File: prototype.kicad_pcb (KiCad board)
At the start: 2 copper layers, 101.5 x 83 mm, 20 parts, among them CON1 SNES-CONN, IC1 SN74LVC4245A, IC2 SN74LVC4245A, IC3 SN74LVC4245A, IC4 SN74LVC4245A, IC5 SN74LVC4245A, IC6 SN74LVC4245A, IC7 SN74LVC4245A, U1 AMS1117-3.3

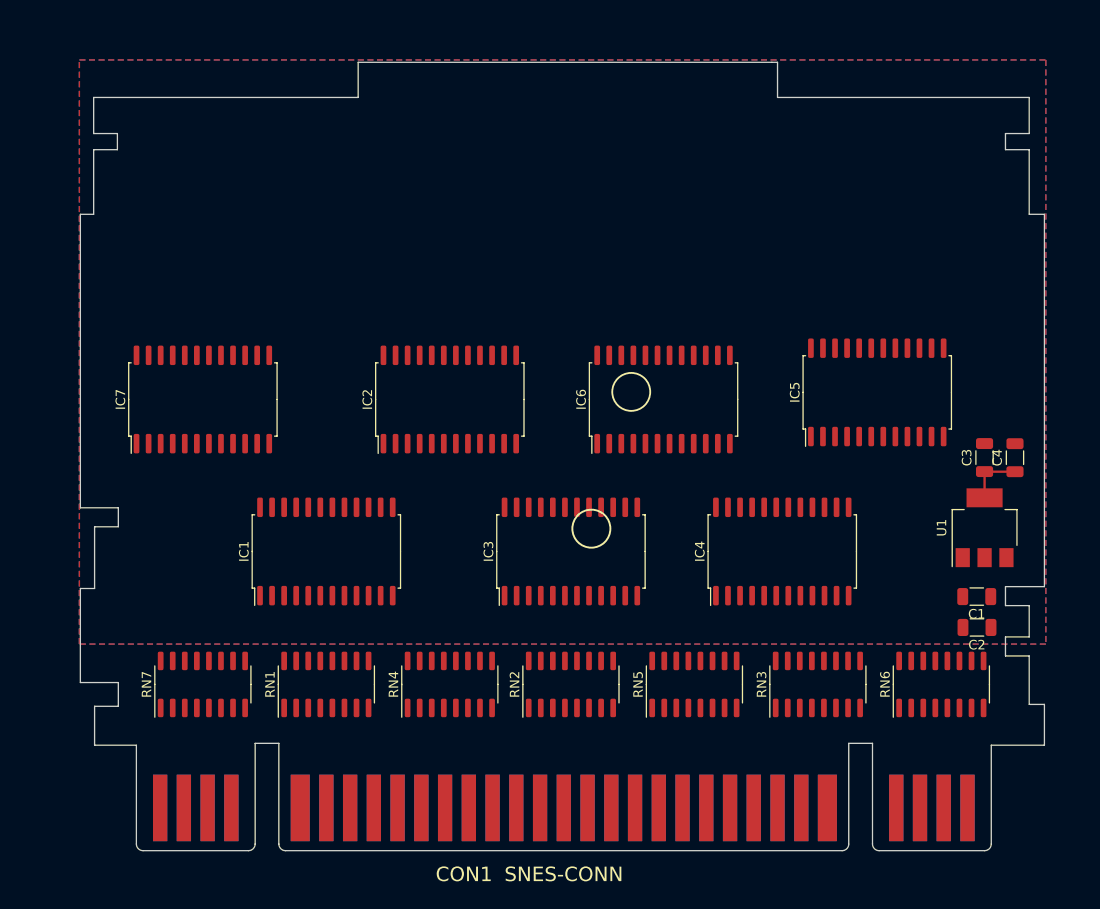
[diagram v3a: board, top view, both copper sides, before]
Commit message: Redesign to reduce components, include PIC12 for CIC implementation
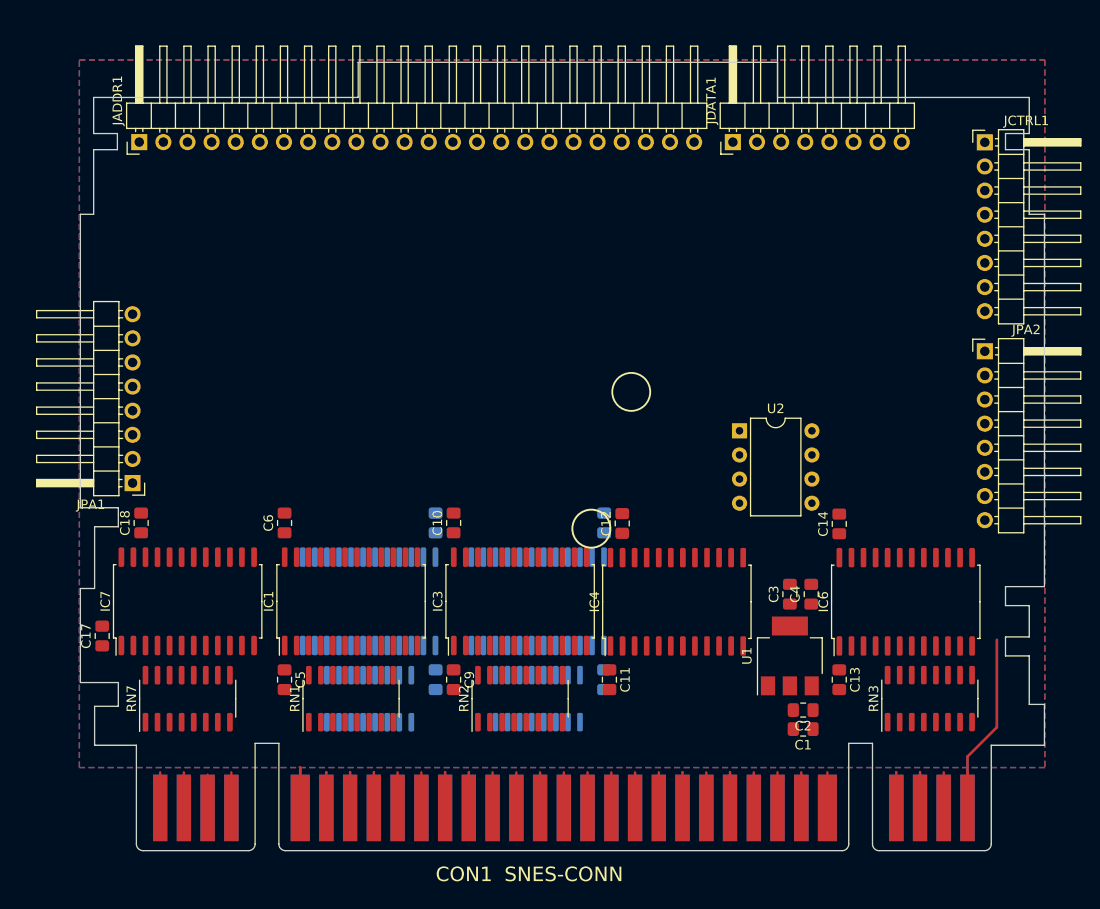
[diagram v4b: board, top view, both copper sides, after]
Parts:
- removed RN6: R_Pack08, Package_SO:SOIC-16_3.9x9.9mm_P1.27mm
- added C10: 0.1uF, Capacitor_SMD:C_0805_2012Metric_Pad1.18x1.45mm_HandSolder, F.Cu at (139.4, 100.5)
- added C11: 0.1uF, Capacitor_SMD:C_0805_2012Metric_Pad1.18x1.45mm_HandSolder, F.Cu at (155.8, 117.0)
- added C12: 0.1uF, Capacitor_SMD:C_0805_2012Metric_Pad1.18x1.45mm_HandSolder, F.Cu at (157.2, 100.5)
- added C13: 0.1uF, Capacitor_SMD:C_0805_2012Metric_Pad1.18x1.45mm_HandSolder, F.Cu at (180.0, 117.0)
- added C14: 0.1uF, Capacitor_SMD:C_0805_2012Metric_Pad1.18x1.45mm_HandSolder, F.Cu at (180.0, 100.6)
- added C15: 0.1uF, Capacitor_SMD:C_0805_2012Metric_Pad1.18x1.45mm_HandSolder, B.Cu at (155.2, 117.0)
- added C16: 0.1uF, Capacitor_SMD:C_0805_2012Metric_Pad1.18x1.45mm_HandSolder, B.Cu at (155.2, 100.5)
- added C17: 0.1uF, Capacitor_SMD:C_0805_2012Metric_Pad1.18x1.45mm_HandSolder, F.Cu at (102.4, 112.4)
- added C18: 0.1uF, Capacitor_SMD:C_0805_2012Metric_Pad1.18x1.45mm_HandSolder, F.Cu at (106.5, 100.5)
- added C5: 0.1uF, Capacitor_SMD:C_0805_2012Metric_Pad1.18x1.45mm_HandSolder, F.Cu at (121.6, 117.0)
- added C6: 0.1uF, Capacitor_SMD:C_0805_2012Metric_Pad1.18x1.45mm_HandSolder, F.Cu at (121.6, 100.5)
- added C7: 0.1uF, Capacitor_SMD:C_0805_2012Metric_Pad1.18x1.45mm_HandSolder, B.Cu at (137.5, 117.0)
- added C8: 0.1uF, Capacitor_SMD:C_0805_2012Metric_Pad1.18x1.45mm_HandSolder, B.Cu at (137.5, 100.5)
- added C9: 0.1uF, Capacitor_SMD:C_0805_2012Metric_Pad1.18x1.45mm_HandSolder, F.Cu at (139.4, 117.0)
- added JADDR1: Conn_01x24, Connector_PinHeader_2.54mm:PinHeader_1x24_P2.54mm_Horizontal, F.Cu at (106.3, 60.4)
- added JCTRL1: Conn_01x08, Connector_PinHeader_2.54mm:PinHeader_1x08_P2.54mm_Horizontal, F.Cu at (195.3, 60.4)
- added JDATA1: Conn_01x08, Connector_PinHeader_2.54mm:PinHeader_1x08_P2.54mm_Horizontal, F.Cu at (168.8, 60.4)
- added JPA1: Conn_01x08, Connector_PinHeader_2.54mm:PinHeader_1x08_P2.54mm_Horizontal, F.Cu at (105.6, 96.3)
- added JPA2: Conn_01x08, Connector_PinHeader_2.54mm:PinHeader_1x08_P2.54mm_Horizontal, F.Cu at (195.3, 82.4)
- added U2: PIC12F629-ISN, Package_DIP:DIP-8_W7.62mm, F.Cu at (169.5, 90.8)
- C1, C2, C3, C4: footprint Capacitor_SMD:C_1206_3216Metric -> Capacitor_SMD:C_0805_2012Metric_Pad1.18x1.45mm_HandSolder
- IC2, IC5, RN4, RN5: moved to B.Cu
- moved IC5 42.0 mm to (148.2, 108.8)
- moved IC6 33.2 mm to (187.0, 108.8)
- moved C4 25.8 mm to (177.1, 108.0)
- moved C3 25.0 mm to (174.8, 108.0)
- moved U1 24.5 mm to (174.8, 114.5)
- moved C1 23.0 mm to (176.2, 122.2)
- moved IC2 22.9 mm to (130.5, 108.8)
- moved IC7 21.3 mm to (111.4, 108.8)
- moved C2 20.3 mm to (176.2, 120.2)
- moved RN5 16.6 mm to (148.3, 119.0)
- moved IC4 12.3 mm to (162.9, 108.8)
- moved RN3 11.9 mm to (189.5, 119.0)
- moved RN4 8.63 mm to (130.5, 119.0)
- moved IC3 7.50 mm to (146.4, 108.8)
- moved IC1 5.86 mm to (128.6, 108.8)
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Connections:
- net Net-(RN7-Pad1) renamed C_CLK_21.477MHZ
- net Net-(RN7-Pad2) renamed C_EXPAND
- net Net-(RN7-Pad3) renamed C_PA6
- net Net-(RN7-Pad4) renamed C_~{PARD}
- net Net-(RN7-Pad5) renamed C_~{WRAM}
- net Net-(RN7-Pad6) renamed C_REFRESH
- net Net-(RN7-Pad7) renamed C_PA7
- net Net-(RN7-Pad8) renamed C_~{PAWR}
- CON1 pad 18: Net-(CON1-Pad18) -> ~{IRQ}
- CON1 pad 19: Net-(CON1-Pad19) -> D0
- CON1 pad 20: Net-(CON1-Pad20) -> D1
- CON1 pad 21: Net-(CON1-Pad21) -> D2
- CON1 pad 22: Net-(CON1-Pad22) -> D3
- CON1 pad 24: Net-(CON1-Pad24) -> CIC_OUT
- CON1 pad 25: Net-(CON1-Pad25) -> CIC_RST
- CON1 pad 26: Net-(CON1-Pad26) -> ~{RESET}
- CON1 pad 28: Net-(CON1-Pad28) -> C_PA0
- CON1 pad 29: Net-(CON1-Pad29) -> C_PA2
- CON1 pad 30: Net-(CON1-Pad30) -> C_PA4
- CON1 pad 31: unconnected-(CON1-Pad31) -> AUDIO_L
- CON1 pad 50: Net-(CON1-Pad50) -> D4
- CON1 pad 51: Net-(CON1-Pad51) -> D5
- CON1 pad 52: Net-(CON1-Pad52) -> D6
- CON1 pad 53: Net-(CON1-Pad53) -> D7
- CON1 pad 55: Net-(CON1-Pad55) -> CIC_IN
- CON1 pad 56: Net-(CON1-Pad56) -> CIC_CLK
- CON1 pad 59: Net-(CON1-Pad59) -> C_PA1
- CON1 pad 60: Net-(CON1-Pad60) -> C_PA3
- CON1 pad 61: Net-(CON1-Pad61) -> C_PA5
- CON1 pad 62: unconnected-(CON1-Pad62) -> AUDIO_R
- IC1 pad 14: unconnected-(IC1-Pad14) -> EXT_A4
- IC1 pad 15: unconnected-(IC1-Pad15) -> EXT_A5
- IC1 pad 16: unconnected-(IC1-Pad16) -> EXT_A6
- IC1 pad 17: unconnected-(IC1-Pad17) -> EXT_A7
- IC1 pad 18: unconnected-(IC1-Pad18) -> EXT_A8
- IC1 pad 19: unconnected-(IC1-Pad19) -> EXT_A9
- IC1 pad 20: unconnected-(IC1-Pad20) -> EXT_A10
- IC1 pad 21: unconnected-(IC1-Pad21) -> EXT_A11
- IC1 pad 23: unconnected-(IC1-Pad23) -> 3V3
- IC1 pad 24: unconnected-(IC1-Pad24) -> 3V3
- IC2 pad 10: A19 -> A12
- IC2 pad 14: unconnected-(IC2-Pad14) -> EXT_A12
- IC2 pad 15: unconnected-(IC2-Pad15) -> EXT_A13
- IC2 pad 16: unconnected-(IC2-Pad16) -> EXT_A14
- IC2 pad 17: unconnected-(IC2-Pad17) -> EXT_A15
- IC2 pad 18: unconnected-(IC2-Pad18) -> EXT_A16
- IC2 pad 19: unconnected-(IC2-Pad19) -> EXT_A17
- IC2 pad 20: unconnected-(IC2-Pad20) -> EXT_A18
- IC2 pad 21: unconnected-(IC2-Pad21) -> EXT_A19
- IC2 pad 23: unconnected-(IC2-Pad23) -> 3V3
- IC2 pad 24: unconnected-(IC2-Pad24) -> 3V3
- IC2 pad 3: A12 -> A19
- IC2 pad 4: A13 -> A18
- IC2 pad 5: A14 -> A17
- IC2 pad 6: A15 -> A16
- IC2 pad 7: A16 -> A15
- IC2 pad 8: A17 -> A14
- IC2 pad 9: A18 -> A13
- IC3 pad 10: A23 -> GND
- IC3 pad 14: unconnected-(IC3-Pad14) -> GND
- IC3 pad 15: unconnected-(IC3-Pad15) -> GND
- IC3 pad 16: unconnected-(IC3-Pad16) -> GND
- IC3 pad 17: unconnected-(IC3-Pad17) -> EXT_~{RD}
- IC3 pad 18: unconnected-(IC3-Pad18) -> EXT_A0
- IC3 pad 19: unconnected-(IC3-Pad19) -> EXT_A1
- IC3 pad 20: unconnected-(IC3-Pad20) -> EXT_A2
- IC3 pad 21: unconnected-(IC3-Pad21) -> EXT_A3
- IC3 pad 23: unconnected-(IC3-Pad23) -> 3V3
- IC3 pad 24: unconnected-(IC3-Pad24) -> 3V3
- IC3 pad 7: A20 -> ~{RD}
- IC3 pad 8: A21 -> GND
- IC3 pad 9: A22 -> GND
- IC4 pad 14: unconnected-(IC4-Pad14) -> EXT_D7
- IC4 pad 15: unconnected-(IC4-Pad15) -> EXT_D6
- IC4 pad 16: unconnected-(IC4-Pad16) -> EXT_D5
- IC4 pad 17: unconnected-(IC4-Pad17) -> EXT_D4
- IC4 pad 18: unconnected-(IC4-Pad18) -> EXT_D3
- IC4 pad 19: unconnected-(IC4-Pad19) -> EXT_D2
- IC4 pad 2: unconnected-(IC4-Pad2) -> DDIR
- IC4 pad 20: unconnected-(IC4-Pad20) -> EXT_D1
- IC4 pad 21: unconnected-(IC4-Pad21) -> EXT_D0
- IC4 pad 23: unconnected-(IC4-Pad23) -> 3V3
- IC4 pad 24: unconnected-(IC4-Pad24) -> 3V3
- IC5 pad 10: CPU_CLK -> A20
- IC5 pad 14: unconnected-(IC5-Pad14) -> EXT_A20
- IC5 pad 15: unconnected-(IC5-Pad15) -> EXT_A21
- IC5 pad 16: unconnected-(IC5-Pad16) -> EXT_A22
- IC5 pad 17: unconnected-(IC5-Pad17) -> EXT_A23
- IC5 pad 18: unconnected-(IC5-Pad18) -> EXT_~{CE}
- IC5 pad 19: unconnected-(IC5-Pad19) -> EXT_~{WR}
- IC5 pad 20: unconnected-(IC5-Pad20) -> EXT_CPU_CLK
- IC5 pad 21: unconnected-(IC5-Pad21) -> GND
- IC5 pad 23: unconnected-(IC5-Pad23) -> 3V3
- IC5 pad 24: unconnected-(IC5-Pad24) -> 3V3
- IC5 pad 3: ~{CE} -> GND
- IC5 pad 4: ~{RD} -> CPU_CLK
- IC5 pad 5: CIC_RST -> ~{WR}
- IC5 pad 6: ~{RESET} -> ~{CE}
- IC5 pad 7: ~{WR} -> A23
- IC5 pad 8: CIC_IN -> A22
- IC5 pad 9: CIC_CLK -> A21
- IC6 pad 14: unconnected-(IC6-Pad14) -> EXT_PA5
- IC6 pad 15: unconnected-(IC6-Pad15) -> EXT_PA3
- IC6 pad 16: unconnected-(IC6-Pad16) -> EXT_PA1
- IC6 pad 17: unconnected-(IC6-Pad17) -> EXT_PA4
- IC6 pad 18: unconnected-(IC6-Pad18) -> EXT_PA2
- IC6 pad 19: unconnected-(IC6-Pad19) -> EXT_PA0
- IC6 pad 20: unconnected-(IC6-Pad20) -> GND
- IC6 pad 21: unconnected-(IC6-Pad21) -> GND
- IC6 pad 23: unconnected-(IC6-Pad23) -> 3V3
- IC6 pad 24: unconnected-(IC6-Pad24) -> 3V3
- IC6 pad 3: PA6 -> GND
- IC6 pad 4: PA7 -> GND
- IC7 pad 10: unconnected-(IC7-Pad10) -> ~{PAWR}
- IC7 pad 14: unconnected-(IC7-Pad14) -> EXT_~{PAWR}
- IC7 pad 15: unconnected-(IC7-Pad15) -> EXT_PA7
- IC7 pad 16: unconnected-(IC7-Pad16) -> EXT_REFRESH
- IC7 pad 17: unconnected-(IC7-Pad17) -> EXT_~{WRAM}
- IC7 pad 18: unconnected-(IC7-Pad18) -> EXT_~{PARD}
- IC7 pad 19: unconnected-(IC7-Pad19) -> EXT_PA6
- IC7 pad 20: unconnected-(IC7-Pad20) -> EXT_EXPAND
- IC7 pad 21: unconnected-(IC7-Pad21) -> EXT_CLK_21.477MHZ
- IC7 pad 23: unconnected-(IC7-Pad23) -> 3V3
- IC7 pad 24: unconnected-(IC7-Pad24) -> 3V3
- IC7 pad 5: ~{PARD} -> PA6
- IC7 pad 6: ~{WRAM} -> ~{PARD}
- IC7 pad 7: REFRESH -> ~{WRAM}
- IC7 pad 8: ~{PAWR} -> REFRESH
- IC7 pad 9: unconnected-(IC7-Pad9) -> PA7
- RN2 pad 10: D1 -> GND
- RN2 pad 11: D0 -> GND
- RN2 pad 12: ~{IRQ} -> ~{RD}
- RN2 pad 5: Net-(CON1-Pad18) -> Net-(CON1-Pad23)
- RN2 pad 6: Net-(CON1-Pad19) -> GND
- RN2 pad 7: Net-(CON1-Pad20) -> GND
- RN2 pad 8: Net-(CON1-Pad21) -> GND
- RN2 pad 9: D2 -> GND
- RN3 pad 1: Net-(CON1-Pad22) -> C_PA0
- RN3 pad 10: PA2 -> GND
- RN3 pad 11: PA0 -> PA5
- RN3 pad 12: ~{RESET} -> PA3
- RN3 pad 13: CIC_RST -> PA1
- RN3 pad 14: CIC_OUT -> PA4
- RN3 pad 15: ~{RD} -> PA2
- RN3 pad 16: D3 -> PA0
- RN3 pad 2: Net-(CON1-Pad23) -> C_PA2
- RN3 pad 3: Net-(CON1-Pad24) -> C_PA4
- RN3 pad 4: Net-(CON1-Pad25) -> C_PA1
- RN3 pad 5: Net-(CON1-Pad26) -> C_PA3
- RN3 pad 6: Net-(CON1-Pad28) -> C_PA5
- RN3 pad 7: Net-(CON1-Pad29) -> GND
- RN3 pad 8: Net-(CON1-Pad30) -> GND
- RN3 pad 9: PA4 -> GND
- RN4 pad 1: Net-(CON1-Pad37) -> Net-(CON1-Pad44)
- RN4 pad 10: A18 -> A13
- RN4 pad 11: A17 -> A14
- RN4 pad 12: A16 -> A15
- RN4 pad 13: A15 -> A16
- RN4 pad 14: A14 -> A17
- RN4 pad 15: A13 -> A18
- RN4 pad 16: A12 -> A19
- RN4 pad 2: Net-(CON1-Pad38) -> Net-(CON1-Pad43)
- RN4 pad 3: Net-(CON1-Pad39) -> Net-(CON1-Pad42)
- RN4 pad 4: Net-(CON1-Pad40) -> Net-(CON1-Pad41)
- RN4 pad 5: Net-(CON1-Pad41) -> Net-(CON1-Pad40)
- RN4 pad 6: Net-(CON1-Pad42) -> Net-(CON1-Pad39)
- RN4 pad 7: Net-(CON1-Pad43) -> Net-(CON1-Pad38)
- RN4 pad 8: Net-(CON1-Pad44) -> Net-(CON1-Pad37)
- RN4 pad 9: A19 -> A12
- RN5 pad 1: Net-(CON1-Pad45) -> GND
- RN5 pad 10: D5 -> A21
- RN5 pad 11: D4 -> A22
- RN5 pad 12: ~{CE} -> A23
- RN5 pad 13: A23 -> ~{CE}
- RN5 pad 14: A22 -> ~{WR}
- RN5 pad 15: A21 -> CPU_CLK
- RN5 pad 16: A20 -> GND
- RN5 pad 2: Net-(CON1-Pad46) -> Net-(CON1-Pad57)
- RN5 pad 3: Net-(CON1-Pad47) -> Net-(CON1-Pad54)
- RN5 pad 4: Net-(CON1-Pad48) -> Net-(CON1-Pad49)
- RN5 pad 5: Net-(CON1-Pad49) -> Net-(CON1-Pad48)
- RN5 pad 6: Net-(CON1-Pad50) -> Net-(CON1-Pad47)
- RN5 pad 7: Net-(CON1-Pad51) -> Net-(CON1-Pad46)
- RN5 pad 8: Net-(CON1-Pad52) -> Net-(CON1-Pad45)
- RN5 pad 9: D6 -> A20
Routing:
- net AUDIO_L: track 0.00 -> 22.7 mm
- net AUDIO_R: track 0.00 -> 19.0 mm
- net GND: track 0.00 -> 8.57 mm
- net 3V3: track 5.97 -> 0.00 mm
- net C_~{PARD}: track 0.00 -> 3.75 mm
- net Net-(CON1-Pad6): track 0.00 -> 3.75 mm
- net C_PA0: track 0.00 -> 3.75 mm
- net Net-(CON1-Pad7): track 0.00 -> 3.75 mm
- net Net-(CON1-Pad11): track 0.00 -> 3.75 mm
- net D2: track 0.00 -> 3.75 mm
- net Net-(CON1-Pad23): track 0.00 -> 3.75 mm
- net C_PA2: track 0.00 -> 3.75 mm
- net Net-(CON1-Pad8): track 0.00 -> 3.75 mm
- net Net-(CON1-Pad12): track 0.00 -> 3.75 mm
- net Net-(CON1-Pad16): track 0.00 -> 3.75 mm
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
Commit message: Routed PCB; fixed up labels on schematic for proper input/output direction; added back in IRQ and RESET as inputs, can easily pull down with mosfet later
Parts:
- moved U2 11.3 mm to (180.0, 86.5)
- moved C15 4.72 mm to (158.3, 113.4), turned to 0 degrees
- moved C18 0.40 mm to (106.5, 100.1)
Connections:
- C10 pad 1: 3V3 -> +3.3V
- C12 pad 1: 3V3 -> +3.3V
- C14 pad 1: 3V3 -> +3.3V
- C16 pad 1: 3V3 -> +3.3V
- C18 pad 1: 3V3 -> +3.3V
- C3 pad 1: 3V3 -> +3.3V
- C4 pad 1: 3V3 -> +3.3V
- C6 pad 1: 3V3 -> +3.3V
- C8 pad 1: 3V3 -> +3.3V
- CON1 pad 18: ~{IRQ} -> Net-(RN2-Pad5)
- CON1 pad 26: ~{RESET} -> Net-(RN2-Pad7)
- IC1 pad 23: 3V3 -> +3.3V
- IC1 pad 24: 3V3 -> +3.3V
- IC2 pad 23: 3V3 -> +3.3V
- IC2 pad 24: 3V3 -> +3.3V
- IC3 pad 15: GND -> EXT_~{RESET}
- IC3 pad 16: GND -> EXT_~{RD}
- IC3 pad 17: EXT_~{RD} -> EXT_~{IRQ}
- IC3 pad 23: 3V3 -> +3.3V
- IC3 pad 24: 3V3 -> +3.3V
- IC3 pad 7: ~{RD} -> ~{IRQ}
- IC3 pad 8: GND -> ~{RD}
- IC3 pad 9: GND -> ~{RESET}
- IC4 pad 23: 3V3 -> +3.3V
- IC4 pad 24: 3V3 -> +3.3V
- IC5 pad 23: 3V3 -> +3.3V
- IC5 pad 24: 3V3 -> +3.3V
- IC6 pad 23: 3V3 -> +3.3V
- IC6 pad 24: 3V3 -> +3.3V
- IC7 pad 23: 3V3 -> +3.3V
- IC7 pad 24: 3V3 -> +3.3V
- JCTRL1 pad 2: EXT_~{RD} -> EXT_~{IRQ}
- JCTRL1 pad 4: EXT_CPU_CLK -> EXT_~{RD}
- JCTRL1 pad 5: 3V3 -> EXT_CPU_CLK
- JCTRL1 pad 6: ~{IRQ} -> EXT_~{RESET}
- JCTRL1 pad 7: VCC -> +3.3V
- RN2 pad 10: GND -> ~{RESET}
- RN2 pad 11: GND -> ~{RD}
- RN2 pad 12: ~{RD} -> ~{IRQ}
- RN2 pad 5: Net-(CON1-Pad23) -> Net-(RN2-Pad5)
- RN2 pad 6: GND -> Net-(CON1-Pad23)
- RN2 pad 7: GND -> Net-(RN2-Pad7)
- U1 pad 2: 3V3 -> +3.3V
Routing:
- net VCC: track 3.75 -> 242.1 mm
- net +3.3V: track 0.00 -> 177.9 mm, vias 0 -> 1
- net EXT_A12: track 0.00 -> 75.8 mm
- net EXT_A13: track 0.00 -> 75.0 mm
- net EXT_A0: track 0.00 -> 74.8 mm, vias 0 -> 1
- net EXT_A1: track 0.00 -> 74.2 mm, vias 0 -> 1
- net EXT_A2: track 0.00 -> 73.8 mm, vias 0 -> 1
- net EXT_A14: track 0.00 -> 73.3 mm
- net EXT_A3: track 0.00 -> 73.2 mm, vias 0 -> 1
- net EXT_A15: track 0.00 -> 72.0 mm
- net EXT_A16: track 0.00 -> 70.3 mm
- net EXT_~{CE}: track 0.00 -> 70.0 mm
- net EXT_A17: track 0.00 -> 68.6 mm
- net EXT_A18: track 0.00 -> 66.9 mm
- net EXT_A19: track 0.00 -> 65.6 mm
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
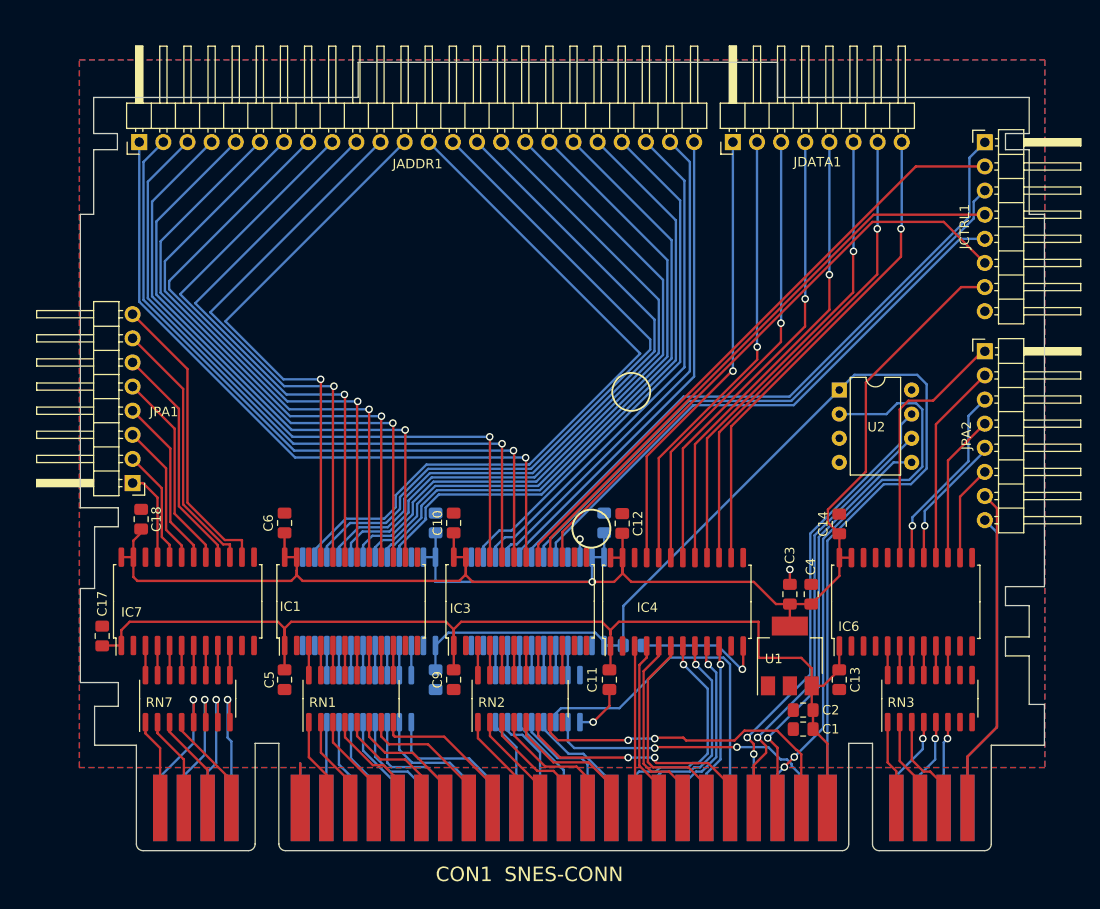
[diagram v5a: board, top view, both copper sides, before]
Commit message: Routed new connector dedicated to power pins; routed DDIR pin to header
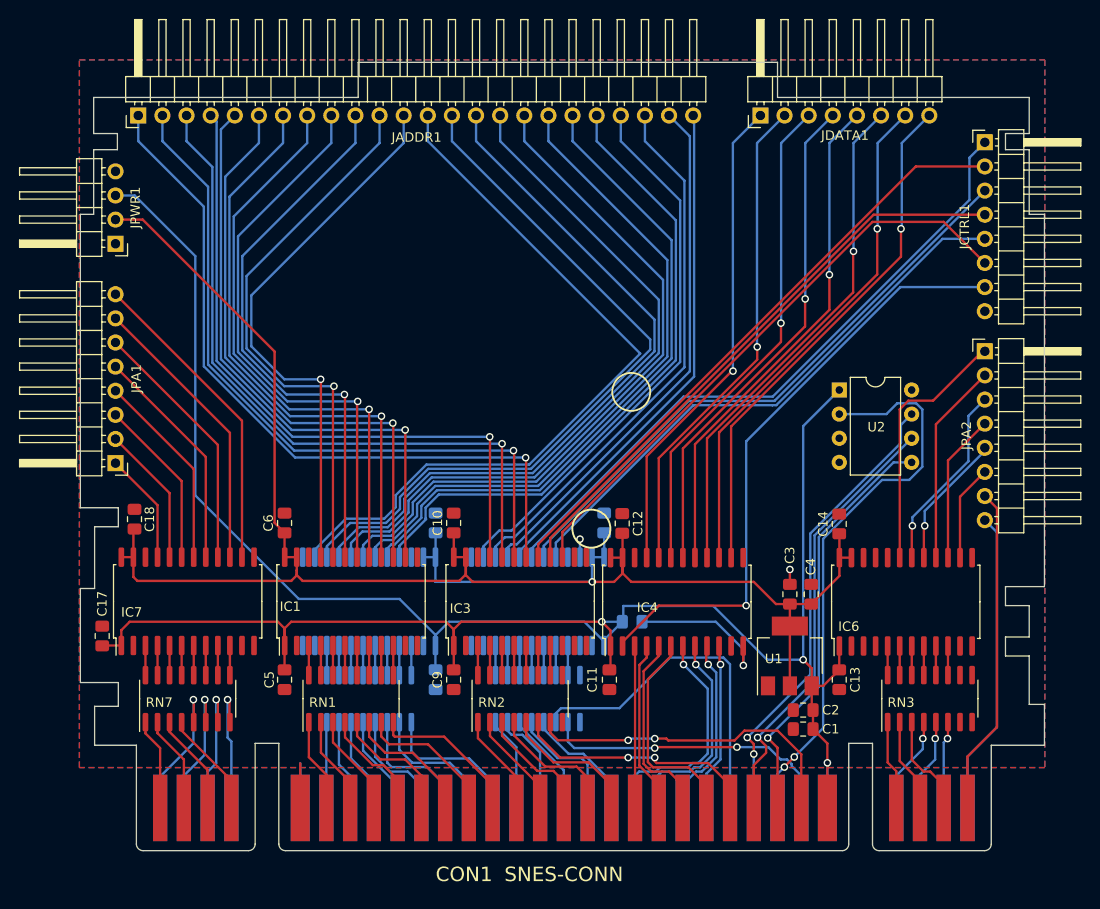
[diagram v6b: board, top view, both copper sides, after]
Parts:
- added JPWR1: Conn_01x04, Connector_PinHeader_2.54mm:PinHeader_1x04_P2.54mm_Horizontal, F.Cu at (103.8, 71.1)
- moved JDATA1 4.03 mm to (171.7, 57.6)
- moved JADDR1 2.80 mm to (106.2, 57.6)
- moved JPA1 2.77 mm to (103.8, 94.2)
- moved C15 2.50 mm to (158.2, 110.9)
- moved C18 0.70 mm to (105.8, 100.1)
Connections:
- IC3 pad 10: GND -> unconnected-(IC3-Pad10)
- IC3 pad 14: GND -> unconnected-(IC3-Pad14)
- IC4 pad 2: DDIR -> EXT_DDIR
- JCTRL1 pad 7: +3.3V -> EXT_DDIR
- JCTRL1 pad 8: GND -> unconnected-(JCTRL1-Pad8)
- RN2 pad 8: GND -> unconnected-(RN2-Pad8)
- RN2 pad 9: GND -> unconnected-(RN2-Pad9)
- RN5 pad 1: GND -> unconnected-(RN5-Pad1)
- RN5 pad 16: GND -> unconnected-(RN5-Pad16)
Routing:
- net EXT_DDIR: track 0.00 -> 64.2 mm, vias 0 -> 1
- net +3.3V: track 177.9 -> 191.6 mm
- net VCC: track 242.1 -> 251.4 mm, vias 0 -> 3
- net GND: track 35.5 -> 28.5 mm, vias 4 -> 3
- net EXT_D6: track 50.7 -> 54.7 mm
- net EXT_D4: track 49.6 -> 53.6 mm
- net EXT_D3: track 49.1 -> 53.1 mm
- net EXT_D2: track 48.6 -> 52.6 mm
- net EXT_D1: track 48.1 -> 52.1 mm
- net EXT_D5: track 50.1 -> 54.1 mm
- net EXT_D0: track 47.6 -> 51.6 mm
- net EXT_D7: track 51.2 -> 55.2 mm
- net EXT_A4: track 65.0 -> 62.1 mm
- net EXT_A5: track 64.5 -> 61.6 mm
- net EXT_A6: track 64.0 -> 61.1 mm
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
